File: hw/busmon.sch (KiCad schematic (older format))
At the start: 19 parts, among them J1 CONN_01X08, J2 CONN_01X08, J3 DIL14, J4 DIL14, J5 DIL14, J6 DIL14, J7 CONN_01X02, Q1 2N3906, Q2 2N3906

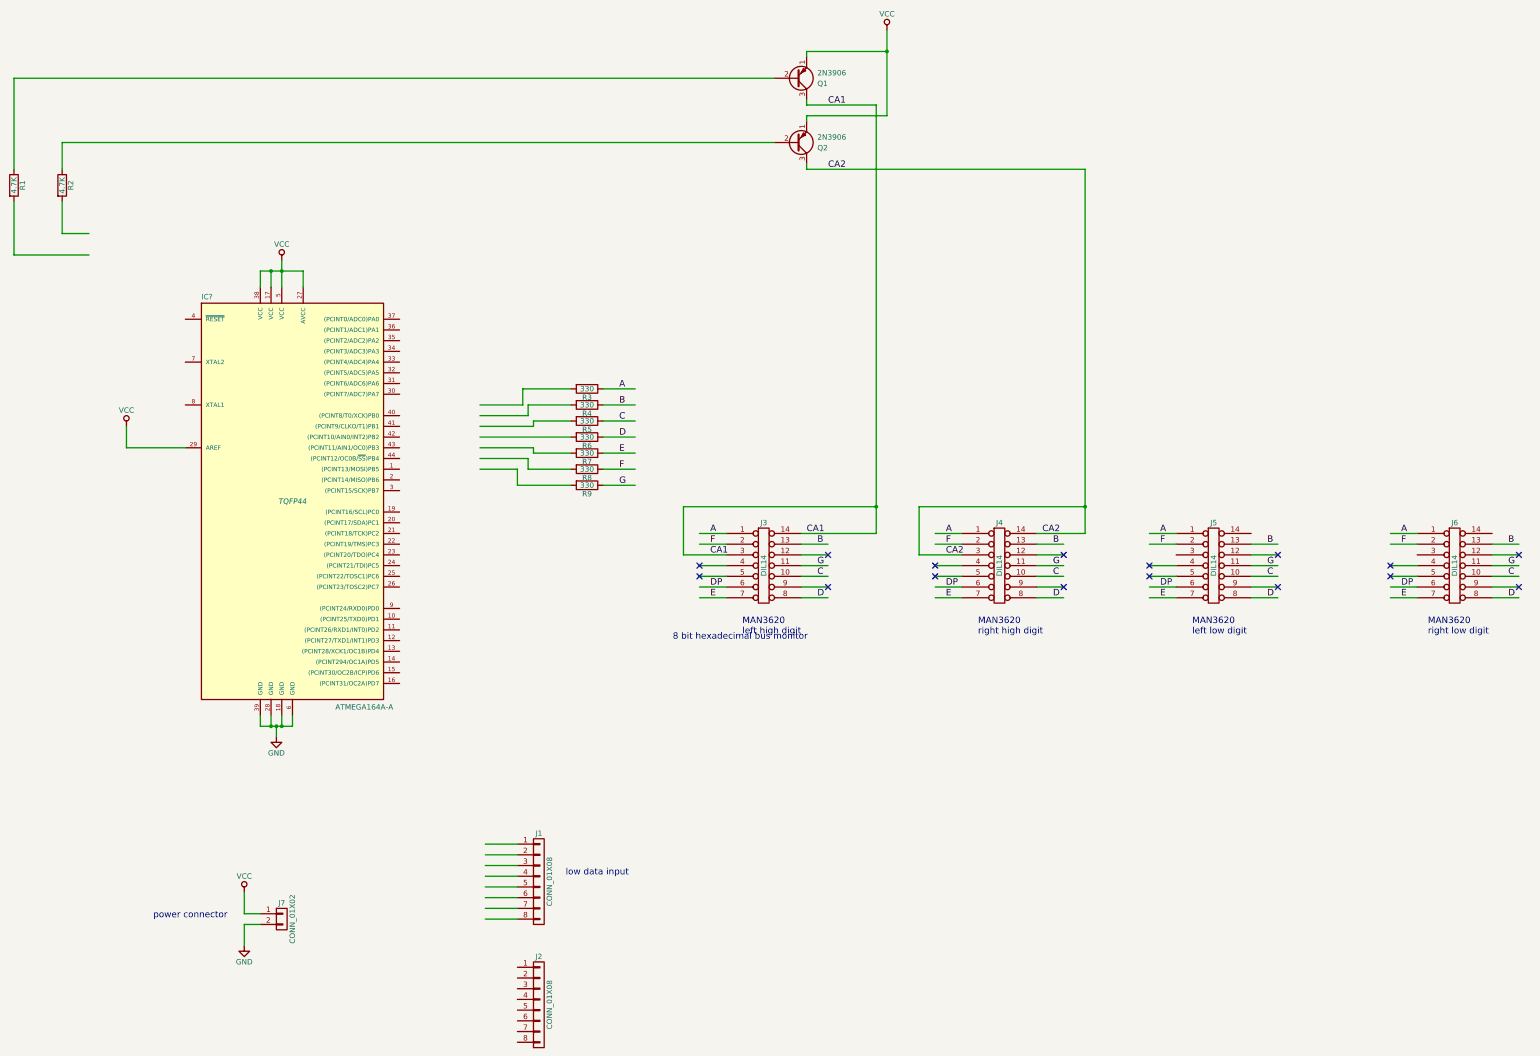
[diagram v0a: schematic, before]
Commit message: connected components
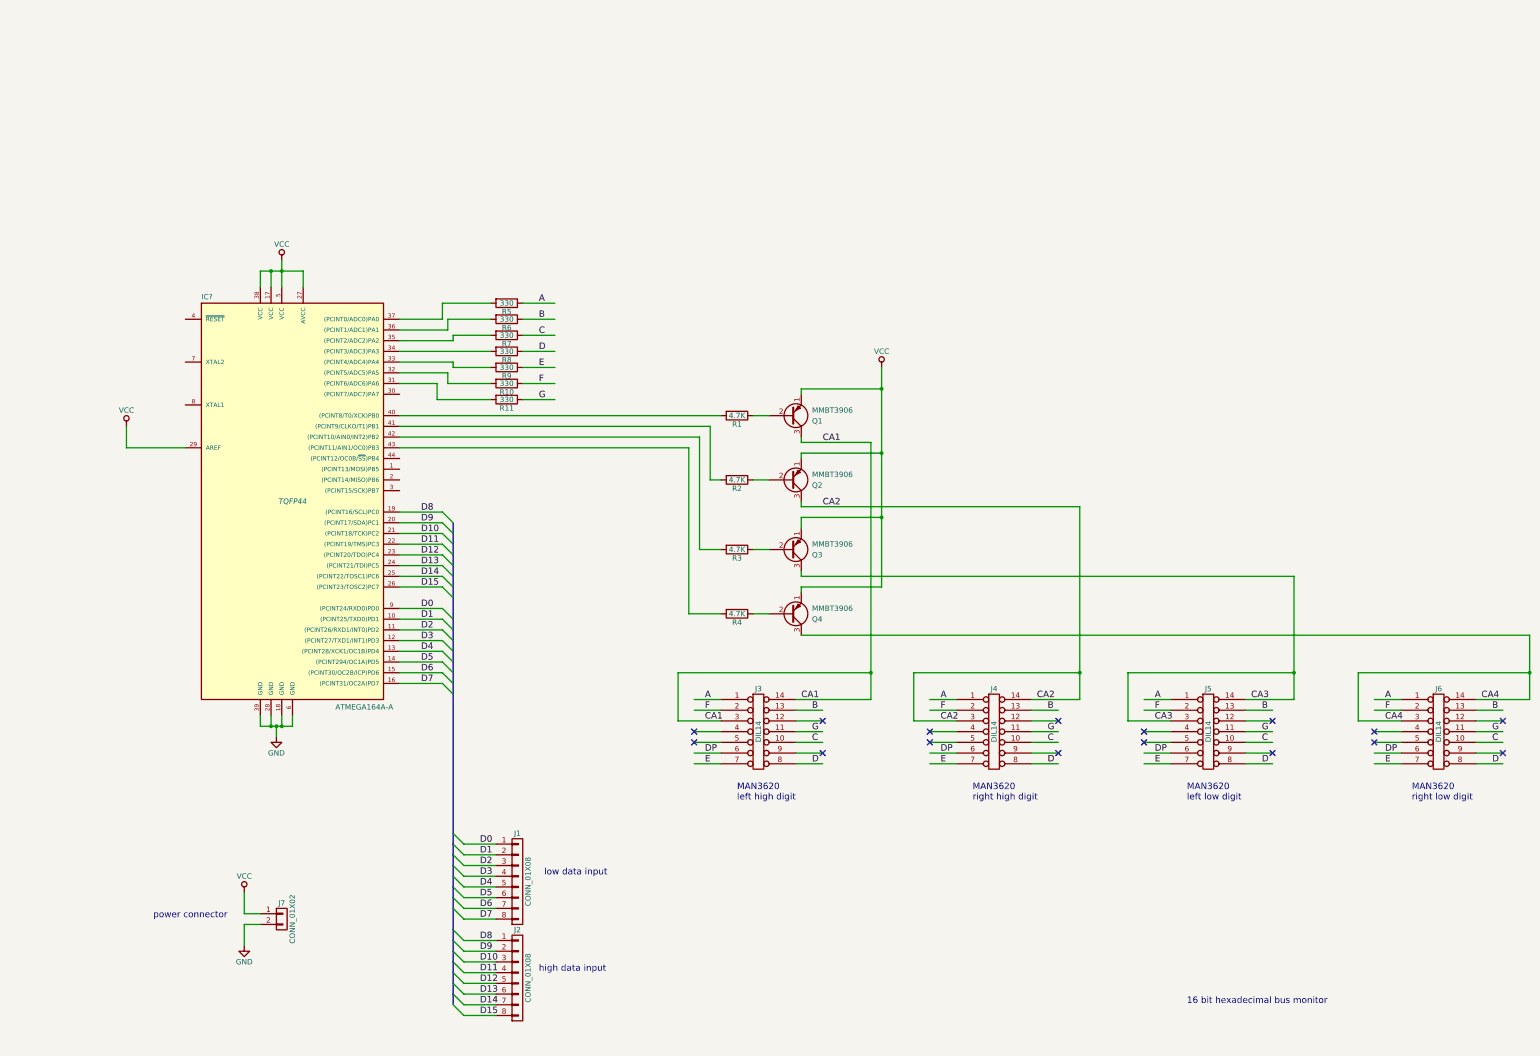
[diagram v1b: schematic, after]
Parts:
- added Q3, Q4: MMBT3906, symbol Q_PNP_EBC
- added R3, R4: 4.7K, symbol R
- Q1, Q2: value 2N3906 -> MMBT3906
- renumbered R8 to R10, R9 to R11, R3 to R5, R4 to R6, R5 to R7, R6 to R8, R7 to R9
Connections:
- net labels added: CA3, CA4, D0, D1, D10, D11, D12, D13, D14, D15, D2, D3, D4, D5, D6, D7, D8, D9
- wire segments 126 -> 186
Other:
- note added: "16 bit hexadecimal bus monitor"
- note added: "high data input"
- note removed: "8 bit hexadecimal bus monitor"
- moved on the sheet: J1, J2, J3, J4, J5, J6, Q1, Q2, R10, R11, R5, R6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

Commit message: getting ready for pcb
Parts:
- added C1: CP1, symbol CP1
- added J8: CONN_01X06, symbol CONN_01X06
- gave numbers to parts that had none: 1
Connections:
- net labels added: -RST
- wire segments 186 -> 192
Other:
- note added: "decoupling\ncap"
- note added: "power\nconnector"
- note added: "programming\nheader"
- note removed: "power connector"
- moved on the sheet: J1, J2, J3, J4, J5, J6, J7, Q1, Q2, Q3, Q4, R1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

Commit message: associate footprints
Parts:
- C1: footprint (none) -> Capacitors_Tantalum_SMD:CP_Tantalum_Case-A_EIA-3216-18_Hand
- J1, J2: footprint (none) -> Pin_Headers:Pin_Header_Straight_1x08_Pitch2.54mm
- J3, J4, J5, J6: footprint (none) -> Housings_DIP:DIP-14_W7.62mm
- J7: footprint (none) -> Pin_Headers:Pin_Header_Straight_1x02_Pitch2.54mm
- J8: footprint (none) -> Pin_Headers:Pin_Header_Straight_1x06_Pitch2.54mm
- Q1, Q2, Q3, Q4: footprint (none) -> TO_SOT_Packages_SMD:SOT-23-5_HandSoldering
- R1, R10, R11, R2, R3, R4, R5, R6, R7, R8, R9: footprint (none) -> Resistors_SMD:R_0805_HandSoldering
- U1: footprint TQFP44 -> Housings_QFP:TQFP-44_10x10mm_Pitch0.8mm
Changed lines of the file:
@@
 F 0 "J3" H 7650 6800 50  0000 C CNN
 F 1 "DIL14" V 7650 6400 50  0000 C CNN
-F 2 "" H 7650 6400 50  0001 C CNN
+F 2 "Housings_DIP:DIP-14_W7.62mm" H 7650 6400 50  0001 C CNN
 F 3 "" H 7650 6400 50  0001 C CNN
 	1    7650 6400
@@
 F 0 "J4" H 9850 6800 50  0000 C CNN
 F 1 "DIL14" V 9850 6400 50  0000 C CNN
-F 2 "" H 9850 6400 50  0001 C CNN
+F 2 "Housings_DIP:DIP-14_W7.62mm" H 9850 6400 50  0001 C CNN
 F 3 "" H 9850 6400 50  0001 C CNN
 	1    9850 6400
@@
 F 0 "J1" H 5400 8250 50  0000 C CNN
 F 1 "CONN_01X08" V 5500 7800 50  0000 C CNN
-F 2 "" H 5400 7800 50  0001 C CNN
+F 2 "Pin_Headers:Pin_Header_Straight_1x08_Pitch2.54mm" H 5400 7800 50  0001 C CNN
 F 3 "" H 5400 7800 50  0001 C CNN
 	1    5400 7800
@@
 F 0 "Q1" H 8150 3500 50  0000 L CNN
 F 1 "MMBT3906" H 8150 3400 50  0000 L CNN
-F 2 "" H 8150 3550 50  0001 C CNN
+F 2 "TO_SOT_Packages_SMD:SOT-23-5_HandSoldering" H 8150 3550 50  0001 C CNN
 F 3 "" H 7950 3450 50  0001 C CNN
 	1    7950 3450
@@
 F 0 "Q2" H 8150 4100 50  0000 L CNN
 F 1 "MMBT3906" H 8150 4000 50  0000 L CNN
-F 2 "" H 8150 4150 50  0001 C CNN
+F 2 "TO_SOT_Packages_SMD:SOT-23-5_HandSoldering" H 8150 4150 50  0001 C CNN
 F 3 "" H 7950 4050 50  0001 C CNN
 	1    7950 4050
@@
 F 0 "R5" V 5380 2400 50  0000 C CNN
 F 1 "330" V 5300 2400 50  0000 C CNN
-F 2 "" V 5230 2400 50  0001 C CNN
+F 2 "Resistors_SMD:R_0805_HandSoldering" V 5230 2400 50  0001 C CNN
 F 3 "" H 5300 2400 50  0001 C CNN
 	1    5300 2400
@@
 F 0 "R6" V 5380 2550 50  0000 C CNN
 F 1 "330" V 5300 2550 50  0000 C CNN
-F 2 "" V 5230 2550 50  0001 C CNN
+F 2 "Resistors_SMD:R_0805_HandSoldering" V 5230 2550 50  0001 C CNN
 F 3 "" H 5300 2550 50  0001 C CNN
 	1    5300 2550
@@
 F 0 "R7" V 5380 2700 50  0000 C CNN
 F 1 "330" V 5300 2700 50  0000 C CNN
-F 2 "" V 5230 2700 50  0001 C CNN
+F 2 "Resistors_SMD:R_0805_HandSoldering" V 5230 2700 50  0001 C CNN
 F 3 "" H 5300 2700 50  0001 C CNN
 	1    5300 2700
@@
 F 0 "R8" V 5380 2850 50  0000 C CNN
 F 1 "330" V 5300 2850 50  0000 C CNN
-F 2 "" V 5230 2850 50  0001 C CNN
+F 2 "Resistors_SMD:R_0805_HandSoldering" V 5230 2850 50  0001 C CNN
 F 3 "" H 5300 2850 50  0001 C CNN
 	1    5300 2850
@@
 F 0 "R9" V 5380 3000 50  0000 C CNN
 F 1 "330" V 5300 3000 50  0000 C CNN
-F 2 "" V 5230 3000 50  0001 C CNN
+F 2 "Resistors_SMD:R_0805_HandSoldering" V 5230 3000 50  0001 C CNN
 F 3 "" H 5300 3000 50  0001 C CNN
 	1    5300 3000
@@
 F 0 "R10" V 5380 3150 50  0000 C CNN
 F 1 "330" V 5300 3150 50  0000 C CNN
-F 2 "" V 5230 3150 50  0001 C CNN
+F 2 "Resistors_SMD:R_0805_HandSoldering" V 5230 3150 50  0001 C CNN
 F 3 "" H 5300 3150 50  0001 C CNN
 	1    5300 3150
@@
 F 0 "R11" V 5380 3300 50  0000 C CNN
 F 1 "330" V 5300 3300 50  0000 C CNN
-F 2 "" V 5230 3300 50  0001 C CNN
+F 2 "Resistors_SMD:R_0805_HandSoldering" V 5230 3300 50  0001 C CNN
 F 3 "" H 5300 3300 50  0001 C CNN
 	1    5300 3300
@@
 F 0 "J7" H 3350 8650 50  0000 C CNN
 F 1 "CONN_01X02" V 3450 8500 50  0000 C CNN
-F 2 "" H 3350 8500 50  0001 C CNN
+F 2 "Pin_Headers:Pin_Header_Straight_1x02_Pitch2.54mm" H 3350 8500 50  0001 C CNN
 F 3 "" H 3350 8500 50  0001 C CNN
 	1    3350 8500
@@
 F 0 "U1" H 2450 6130 50  0000 L BNN
 F 1 "ATMEGA164A-A" H 3700 2300 50  0000 L BNN
-F 2 "TQFP44" H 3300 4250 50  0000 C CIN
+F 2 "Housings_QFP:TQFP-44_10x10mm_Pitch0.8mm" H 3300 4250 50  0000 C CIN
 F 3 "" H 3300 4250 50  0000 C CNN
 	1    3300 4250
@@
 F 0 "J5" H 11850 6800 50  0000 C CNN
 F 1 "DIL14" V 11850 6400 50  0000 C CNN
-F 2 "" H 11850 6400 50  0001 C CNN
+F 2 "Housings_DIP:DIP-14_W7.62mm" H 11850 6400 50  0001 C CNN
 F 3 "" H 11850 6400 50  0001 C CNN
 	1    11850 6400
@@
 F 0 "J6" H 13900 6800 50  0000 C CNN
 F 1 "DIL14" V 13900 6400 50  0000 C CNN
-F 2 "" H 13900 6400 50  0001 C CNN
+F 2 "Housings_DIP:DIP-14_W7.62mm" H 13900 6400 50  0001 C CNN
 F 3 "" H 13900 6400 50  0001 C CNN
 	1    13900 6400
@@
 F 0 "J2" H 5400 9150 50  0000 C CNN
 F 1 "CONN_01X08" V 5500 8700 50  0000 C CNN
-F 2 "" H 5400 8700 50  0000 C CNN
+F 2 "Pin_Headers:Pin_Header_Straight_1x08_Pitch2.54mm" H 5400 8700 50  0001 C CNN
 F 3 "" H 5400 8700 50  0000 C CNN
 	1    5400 8700
@@
 F 0 "Q3" H 8150 4750 50  0000 L CNN
 F 1 "MMBT3906" H 8150 4650 50  0000 L CNN
-F 2 "" H 8150 4800 50  0001 C CNN
+F 2 "TO_SOT_Packages_SMD:SOT-23-5_HandSoldering" H 8150 4800 50  0001 C CNN
 F 3 "" H 7950 4700 50  0001 C CNN
 	1    7950 4700
@@
 F 0 "Q4" H 8150 5350 50  0000 L CNN
 F 1 "MMBT3906" H 8150 5250 50  0000 L CNN
-F 2 "" H 8150 5400 50  0001 C CNN
+F 2 "TO_SOT_Packages_SMD:SOT-23-5_HandSoldering" H 8150 5400 50  0001 C CNN
 F 3 "" H 7950 5300 50  0001 C CNN
 	1    7950 5300
@@
 F 0 "R1" V 7530 3450 50  0000 C CNN
 F 1 "4.7K" V 7450 3450 50  0000 C CNN
-F 2 "" V 7380 3450 50  0001 C CNN
+F 2 "Resistors_SMD:R_0805_HandSoldering" V 7380 3450 50  0001 C CNN
 F 3 "" H 7450 3450 50  0001 C CNN
 	1    7450 3450
@@
 F 0 "R2" V 7530 4050 50  0000 C CNN
 F 1 "4.7K" V 7450 4050 50  0000 C CNN
-F 2 "" V 7380 4050 50  0001 C CNN
+F 2 "Resistors_SMD:R_0805_HandSoldering" V 7380 4050 50  0001 C CNN
 F 3 "" H 7450 4050 50  0001 C CNN
 	1    7450 4050
@@
 F 0 "R3" V 7530 4700 50  0000 C CNN
 F 1 "4.7K" V 7450 4700 50  0000 C CNN
-F 2 "" V 7380 4700 50  0001 C CNN
+F 2 "Resistors_SMD:R_0805_HandSoldering" V 7380 4700 50  0001 C CNN
 F 3 "" H 7450 4700 50  0001 C CNN
 	1    7450 4700
@@
 F 0 "R4" V 7530 5300 50  0000 C CNN
 F 1 "4.7K" V 7450 5300 50  0000 C CNN
-F 2 "" V 7380 5300 50  0001 C CNN
+F 2 "Resistors_SMD:R_0805_HandSoldering" V 7380 5300 50  0001 C CNN
 F 3 "" H 7450 5300 50  0001 C CNN
 	1    7450 5300
@@
 F 0 "C1" H 2725 8600 50  0000 L CNN
 F 1 "CP1" H 2725 8400 50  0000 L CNN
-F 2 "" H 2700 8500 50  0001 C CNN
+F 2 "Capacitors_Tantalum_SMD:CP_Tantalum_Case-A_EIA-3216-18_Hand" H 2700 8500 50  0001 C CNN
 F 3 "" H 2700 8500 50  0001 C CNN
 	1    2700 8500
@@
 F 0 "J8" H 6100 4950 50  0000 C CNN
 F 1 "CONN_01X06" V 6200 4600 50  0000 C CNN
-F 2 "" H 6100 4600 50  0001 C CNN
+F 2 "Pin_Headers:Pin_Header_Straight_1x06_Pitch2.54mm" H 6100 4600 50  0001 C CNN
 F 3 "" H 6100 4600 50  0001 C CNN
 	1    6100 4600
@@
 	5450 4350 5450 5100
 $Comp
-L GND #PWR?
+L GND #PWR07
 U 1 1 593F01FF
 P 5450 5100
-F 0 "#PWR?" H 5450 4850 50  0001 C CNN
+F 0 "#PWR07" H 5450 4850 50  0001 C CNN
 F 1 "GND" H 5450 4950 50  0000 C CNN
 F 2 "" H 5450 5100 50  0001 C CNN
@@
 	5750 4450 5750 4200
 $Comp
-L VCC #PWR?
+L VCC #PWR08
 U 1 1 593F0381
 P 5750 4200
-F 0 "#PWR?" H 5750 4050 50  0001 C CNN
+F 0 "#PWR08" H 5750 4050 50  0001 C CNN
 F 1 "VCC" H 5750 4350 50  0000 C CNN
 F 2 "" H 5750 4200 50  0001 C CNN

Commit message: use SOT23-3 for transistors
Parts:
- Q1, Q2, Q3, Q4: footprint TO_SOT_Packages_SMD:SOT-23-5_HandSoldering -> TO_SOT_Packages_SMD:SOT-23
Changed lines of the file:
@@
 F 0 "Q1" H 8150 3500 50  0000 L CNN
 F 1 "MMBT3906" H 8150 3400 50  0000 L CNN
-F 2 "TO_SOT_Packages_SMD:SOT-23-5_HandSoldering" H 8150 3550 50  0001 C CNN
+F 2 "TO_SOT_Packages_SMD:SOT-23" H 8150 3550 50  0001 C CNN
 F 3 "" H 7950 3450 50  0001 C CNN
 	1    7950 3450
@@
 F 0 "Q2" H 8150 4100 50  0000 L CNN
 F 1 "MMBT3906" H 8150 4000 50  0000 L CNN
-F 2 "TO_SOT_Packages_SMD:SOT-23-5_HandSoldering" H 8150 4150 50  0001 C CNN
+F 2 "TO_SOT_Packages_SMD:SOT-23" H 8150 4150 50  0001 C CNN
 F 3 "" H 7950 4050 50  0001 C CNN
 	1    7950 4050
@@
 F 0 "Q3" H 8150 4750 50  0000 L CNN
 F 1 "MMBT3906" H 8150 4650 50  0000 L CNN
-F 2 "TO_SOT_Packages_SMD:SOT-23-5_HandSoldering" H 8150 4800 50  0001 C CNN
+F 2 "TO_SOT_Packages_SMD:SOT-23" H 8150 4800 50  0001 C CNN
 F 3 "" H 7950 4700 50  0001 C CNN
 	1    7950 4700
@@
 F 0 "Q4" H 8150 5350 50  0000 L CNN
 F 1 "MMBT3906" H 8150 5250 50  0000 L CNN
-F 2 "TO_SOT_Packages_SMD:SOT-23-5_HandSoldering" H 8150 5400 50  0001 C CNN
+F 2 "TO_SOT_Packages_SMD:SOT-23" H 8150 5400 50  0001 C CNN
 F 3 "" H 7950 5300 50  0001 C CNN
 	1    7950 5300
